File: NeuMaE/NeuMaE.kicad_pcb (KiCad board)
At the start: 2 copper layers, 52.1 x 53.8 mm, 20 parts, among them J1 MOTOR, J2 PROGRAM, J3 LED, J4 PWR, J5 EXTRA, Q1 BC337, SW1 FLASH, SW2 RESET, U1 PMIC-LD1117V33(TO-220), U2 ESP8266-12E_ESP-12E

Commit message: update gerber
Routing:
- net +3V3: track 100.7 -> 100.1 mm
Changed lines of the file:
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@@
     (thickness 1.6)
     (drawings 4)
-    (tracks 172)
+    (tracks 171)
     (zones 0)
     (modules 20)
@@
       (outputformat 1)
       (mirror false)
-      (drillshape 1)
+      (drillshape 0)
       (scaleselection 1)
       (outputdirectory ""))
@@
   (segment (start 60.737501 49.775001) (end 60.737501 48.175001) (width 1) (layer F.Cu) (net 5))
   (segment (start 54.102 59.69) (end 55.146225 59.69) (width 1) (layer F.Cu) (net 5))
-  (segment (start 60.737501 47.974499) (end 61.136998 47.575002) (width 1) (layer F.Cu) (net 5))
   (segment (start 60.737501 56.086499) (end 60.737501 47.974499) (width 1) (layer F.Cu) (net 5))
   (segment (start 57.134 59.69) (end 60.737501 56.086499) (width 1) (layer F.Cu) (net 5))

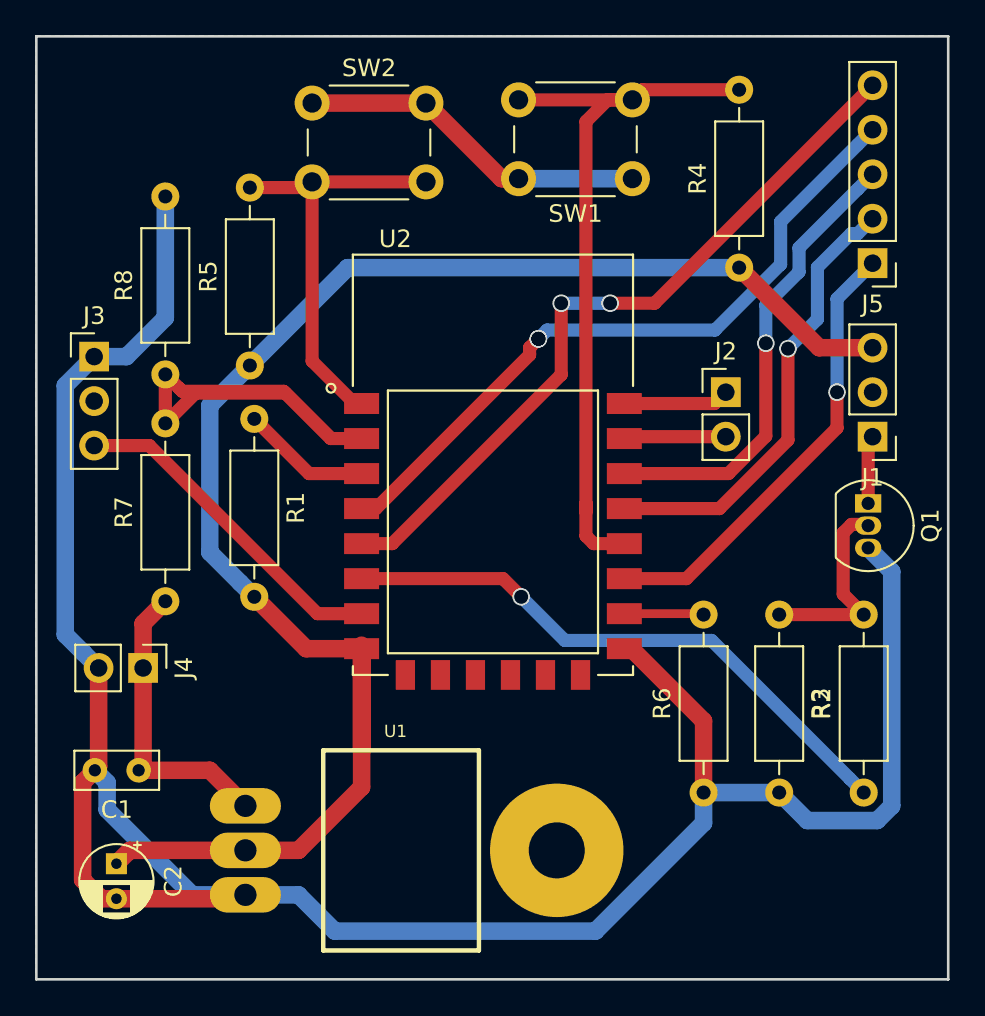
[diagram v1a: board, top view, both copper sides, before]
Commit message: made board smaller
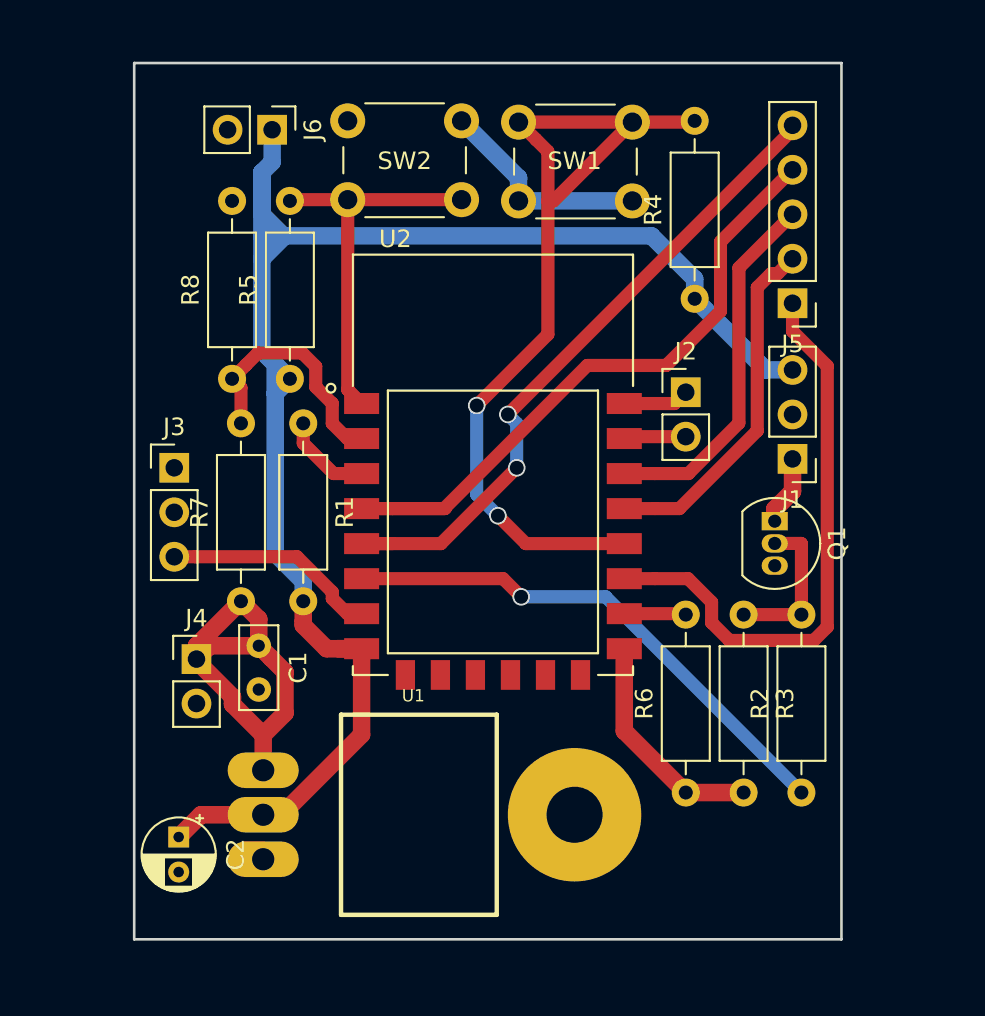
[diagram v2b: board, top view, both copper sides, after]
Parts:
- added J6: PWR, Connector_PinHeader_2.54mm:PinHeader_1x02_P2.54mm_Vertical, F.Cu at (55.6, 18.5)
- moved C1 9.88 mm to (54.9, 48.0), turned to 270 degrees
- moved J3 7.82 mm to (50.0, 37.8)
- moved Q1 5.43 mm to (84.3, 40.9)
- moved J5 5.11 mm to (85.3, 28.4)
- moved J1 4.75 mm to (85.3, 37.3)
- moved R7 4.32 mm to (53.8, 45.5)
- moved C2 3.87 mm to (50.3, 58.9)
- moved R8 3.82 mm to (53.3, 32.8)
- moved R2 3.56 mm to (85.9, 56.4)
- moved R4 3.10 mm to (79.8, 28.2)
- moved J4 3.09 mm to (51.3, 48.8), turned to 0 degrees
- moved R1 2.81 mm to (57.4, 35.3)
- moved R5 2.41 mm to (56.6, 32.8)
- moved J2 2.29 mm to (79.2, 33.5)
- moved SW2 2.27 mm to (59.9, 18.0)
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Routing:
- net GND: track 156.0 -> 28.1 mm
- net /ADC: track 29.3 -> 14.5 mm
- net Net-(R4-Pad2): track 42.9 -> 54.2 mm, vias 0 -> 2
- net Net-(J5-Pad3): track 31.4 -> 20.9 mm, vias 1 -> 0
- net VCC: track 17.2 -> 25.3 mm
- net Net-(J3-Pad3): track 19.2 -> 12.3 mm
- net Net-(J5-Pad2): track 25.8 -> 20.3 mm, vias 1 -> 0
- net Net-(J1-Pad1): track 8.34 -> 3.92 mm
- net Net-(J5-Pad1): track 29.2 -> 33.4 mm, vias 1 -> 0
- net +3V3: track 100.1 -> 96.1 mm
- net /MOTOR: track 33.7 -> 30.2 mm
- net /PIN5: track 42.4 -> 38.9 mm
- net Net-(Q1-Pad2): track 12.0 -> 8.88 mm
- net Net-(J2-Pad1): track 6.06 -> 3.78 mm
- net /RXD: track 5.84 -> 3.55 mm
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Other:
- board size 52.1 x 53.8 mm -> 40.4 x 50 mm

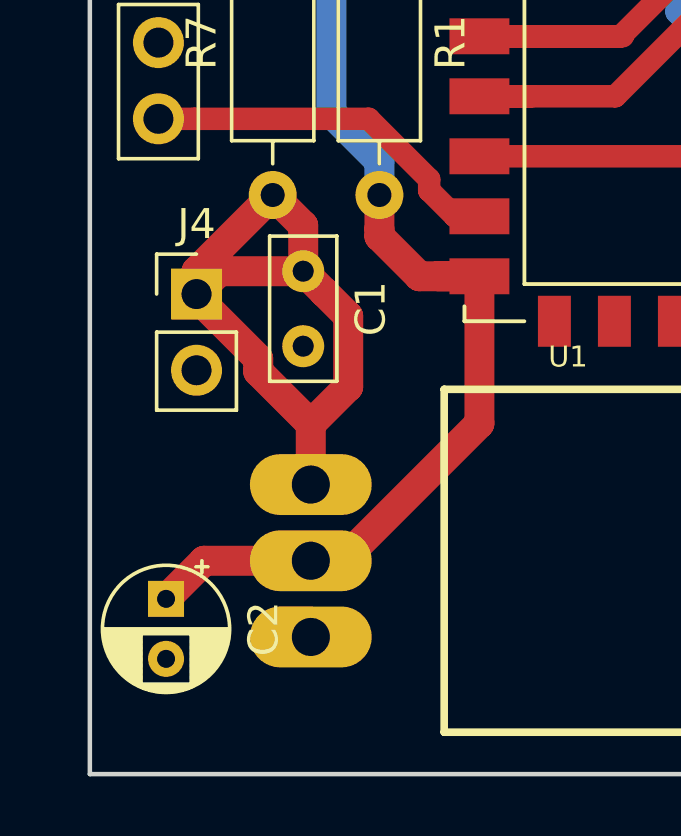
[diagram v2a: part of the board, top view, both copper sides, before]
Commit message: fixed C1 footprint
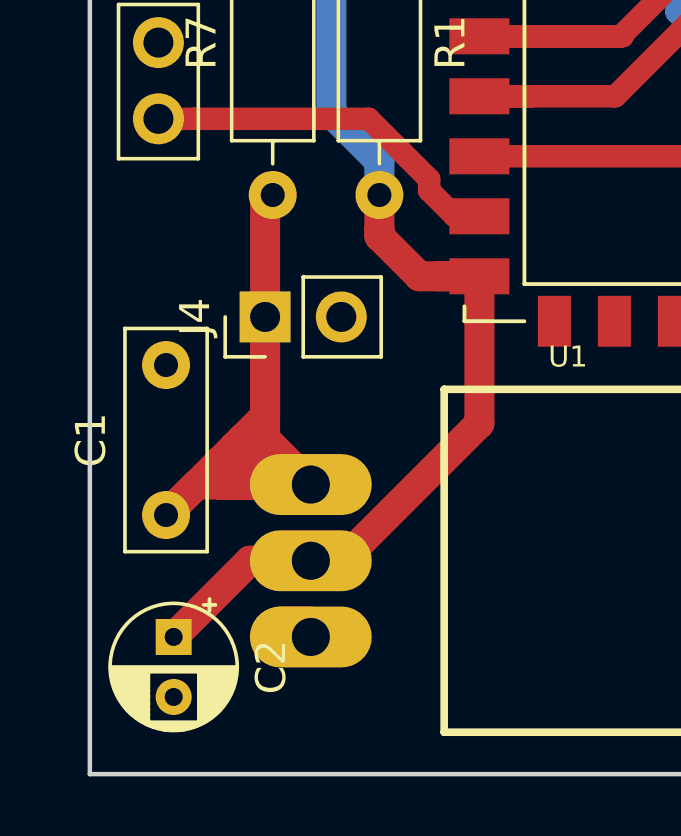
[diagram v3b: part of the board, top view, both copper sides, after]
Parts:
- C1: footprint Capacitor_THT:C_Rect_L4.6mm_W2.0mm_P2.50mm_MKS02_FKP02 -> Capacitor_THT:C_Rect_L7.2mm_W2.5mm_P5.00mm_FKS2_FKP2_MKS2_MKP2
- moved C1 9.33 mm to (50.3, 56.1), turned to 90 degrees
- moved J4 2.41 mm to (53.6, 49.5), turned to 90 degrees
- moved C2 1.30 mm to (50.5, 60.2)
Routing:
- net VCC: track 25.3 -> 35.3 mm

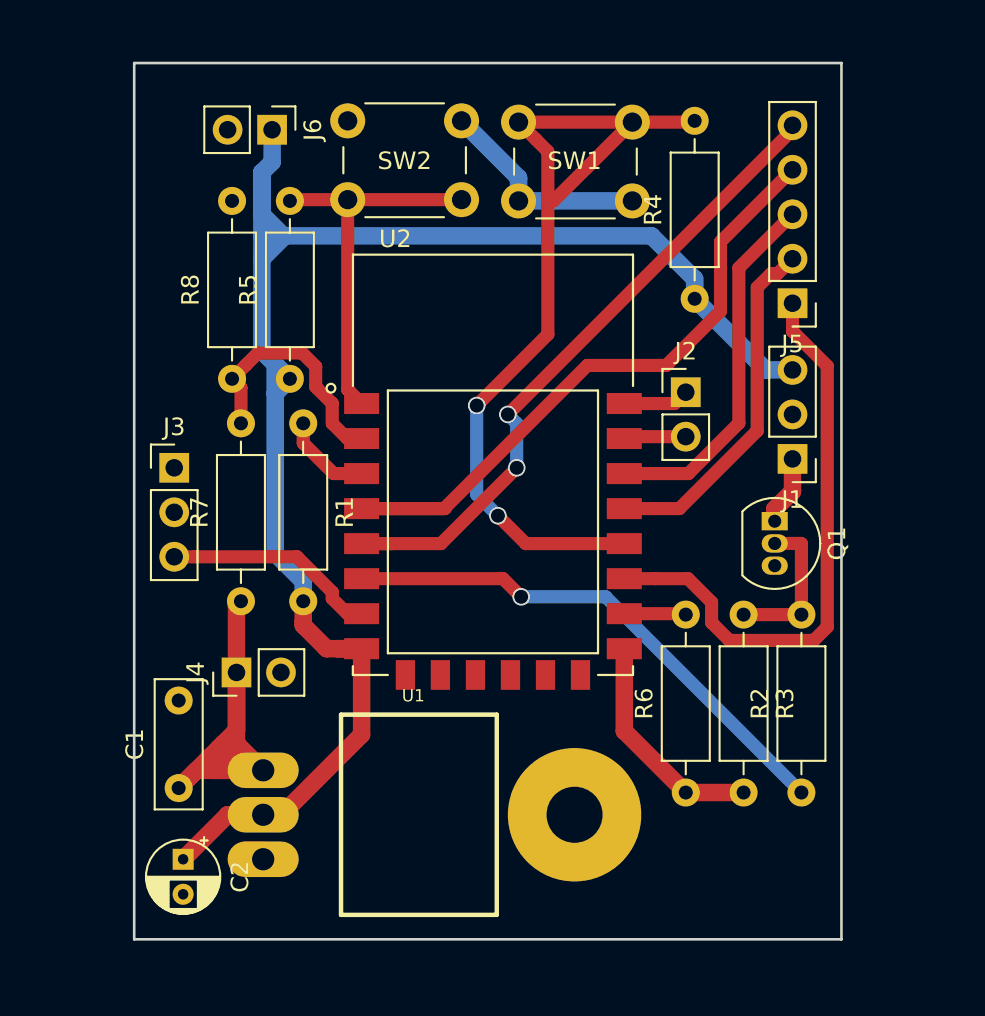
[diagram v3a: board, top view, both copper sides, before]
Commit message: added recoil diode
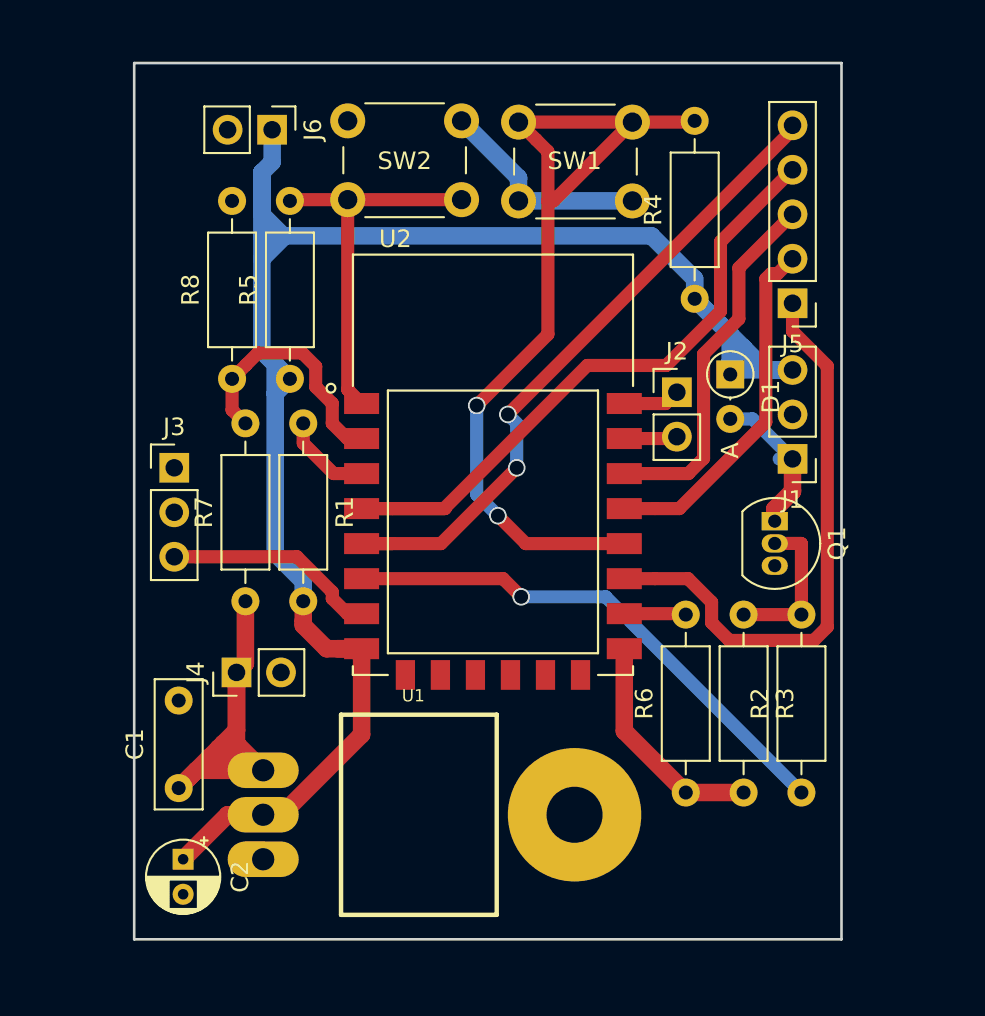
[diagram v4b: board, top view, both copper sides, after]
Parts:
- added D1: RECOIL, Diode_THT:D_DO-35_SOD27_P2.54mm_Vertical_AnodeUp, F.Cu at (81.8, 32.5)
- moved J2 0.51 mm to (78.7, 33.5)
- moved R7 0.25 mm to (54.1, 45.5)
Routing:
- net +3V3: track 96.4 -> 107.1 mm
- net Net-(D1-Pad2): track 3.92 -> 9.19 mm
- net Net-(J2-Pad1): track 3.78 -> 3.27 mm
